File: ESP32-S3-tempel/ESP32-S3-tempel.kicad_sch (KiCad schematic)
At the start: 33 parts, among them J1 USB_C_Receptacle_USB2.0_14P, J2 USB_C_Receptacle_USB2.0_14P, J3 West, J4 East, J5 Nort, J6 South, Q1 SS8050, Q2 SS8050, SW1 RST, SW2 Boot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

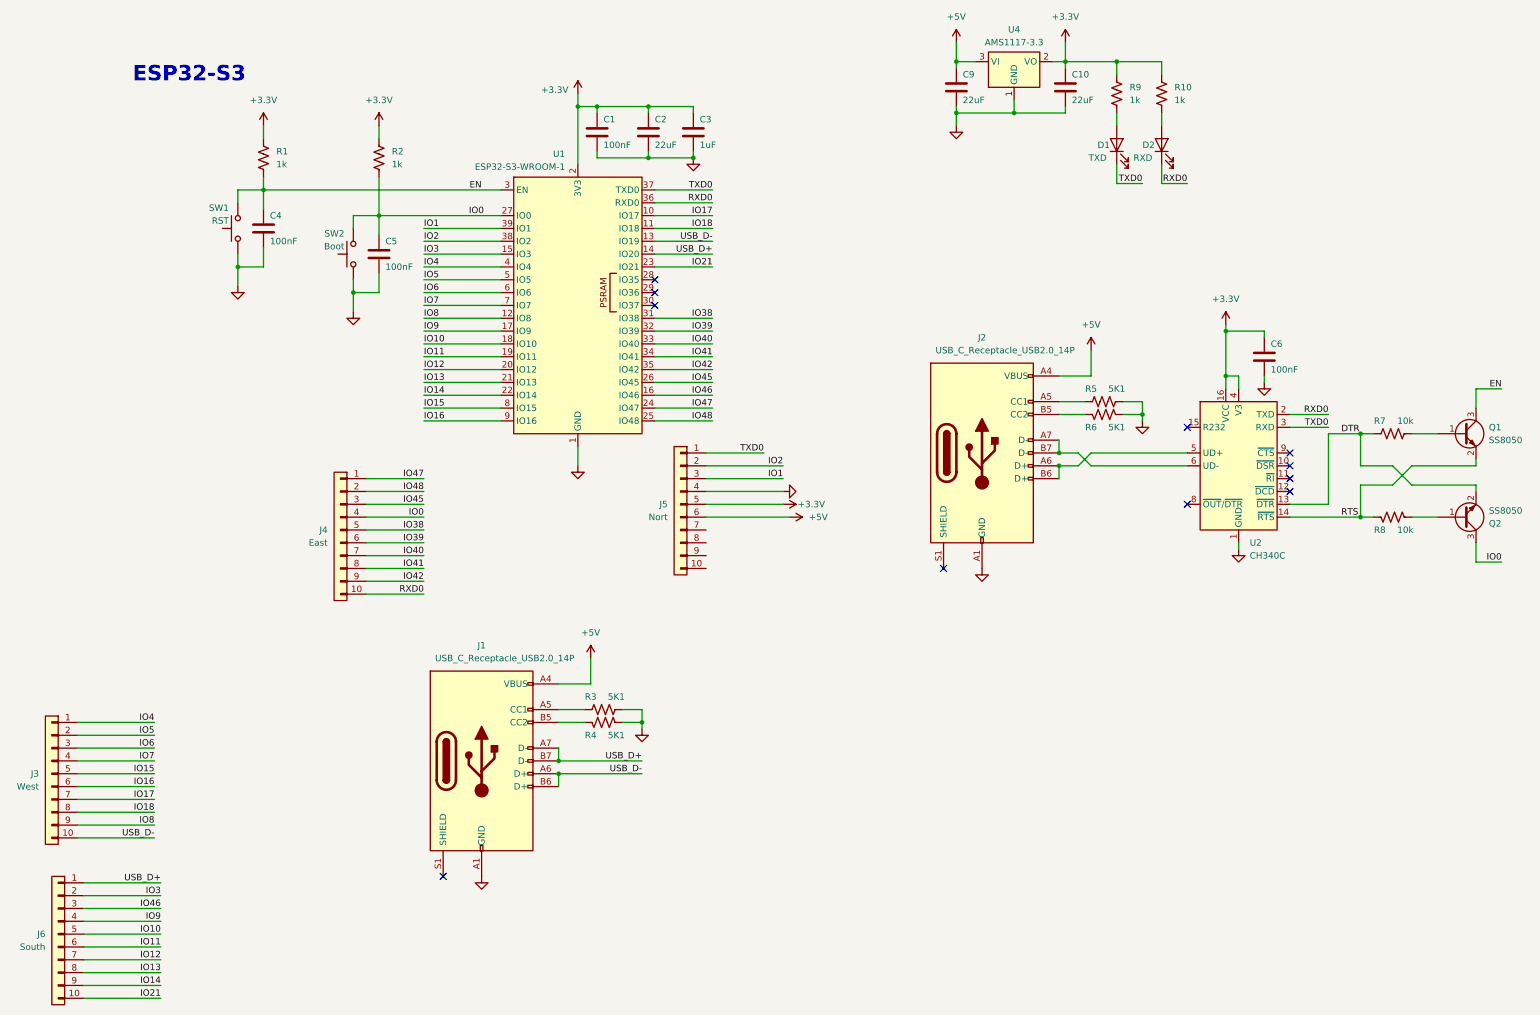
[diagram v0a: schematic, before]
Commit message: feat: finish routing and tidyng silkscreen
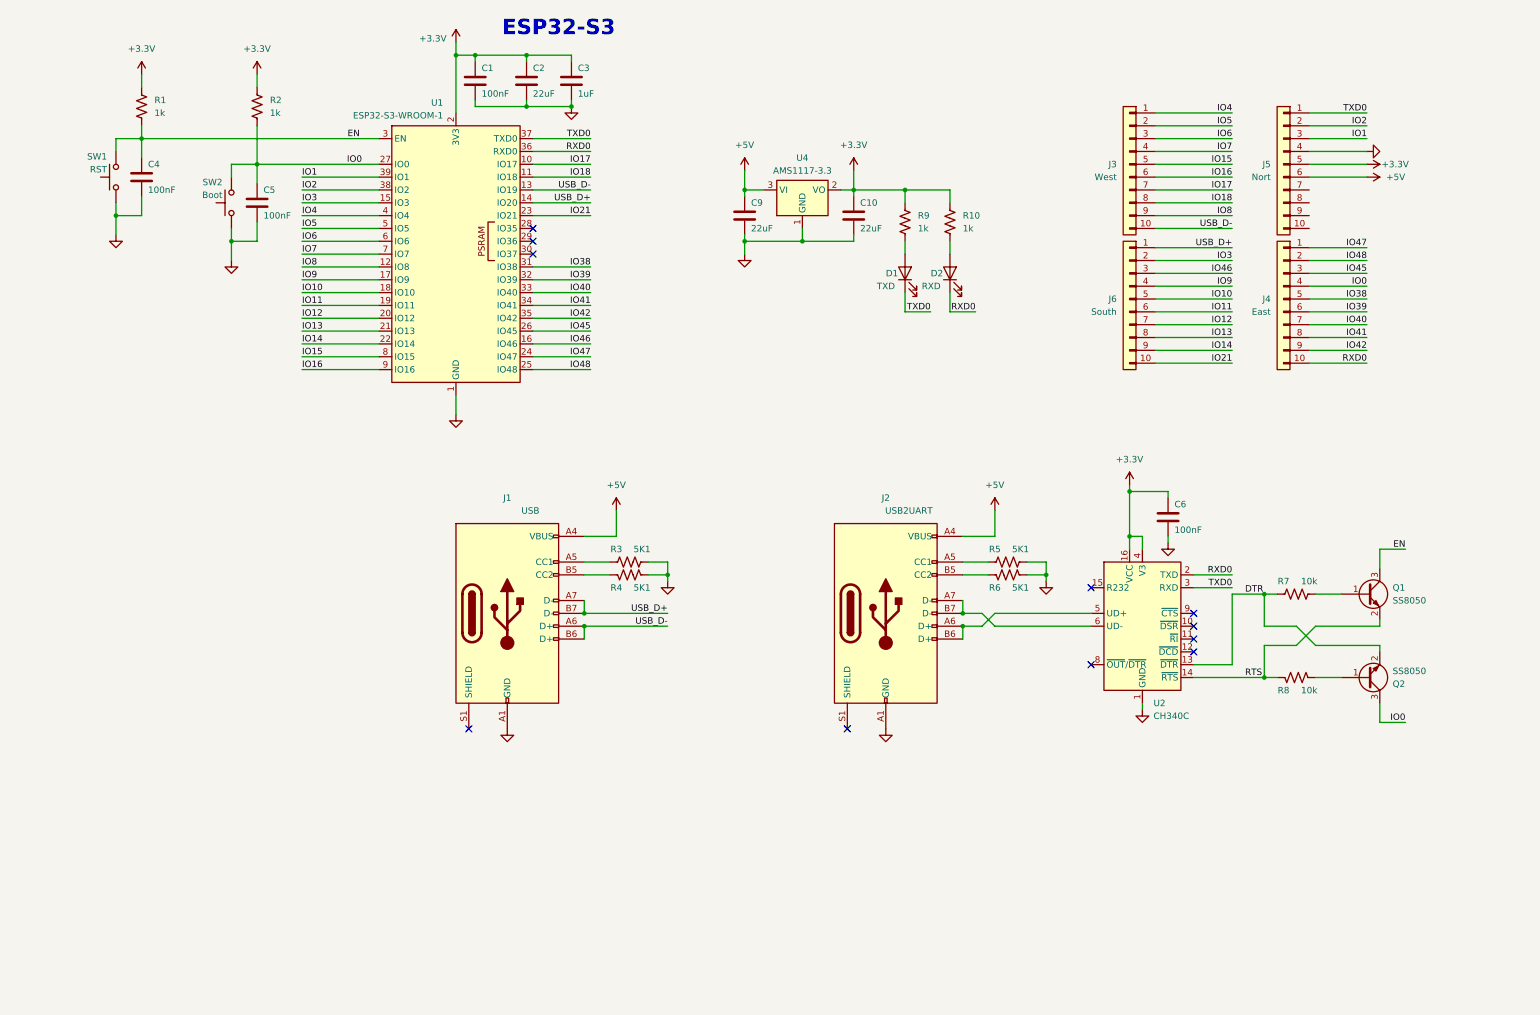
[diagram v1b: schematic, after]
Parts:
- J1: value USB_C_Receptacle_USB2.0_14P -> USB
- J2: value USB_C_Receptacle_USB2.0_14P -> USB2UART
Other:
- title: (none) -> ESP32-S3 Tempel
- moved on the sheet: C1, C10, C2, C3, C4, C5, C6, C9, D1, D2, J1, J2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
